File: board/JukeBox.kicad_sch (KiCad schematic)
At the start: 73 parts, among them J1 USB4105-GF-A, J2 Conn_01x03, J3 Conn_01x04, J4 Conn_01x08, J5 Conn_01x01, J6 Conn_01x03, J7 Conn_01x03, J8 Conn_01x01, SW1 SW_SPST, SW10 SW_SPST, SW11 SW_SPST, SW12 SW_SPST, SW2 SW_SPST, SW3 SW_SPST, SW4 SW_SPST, SW5 SW_SPST, SW6 SW_SPST, SW7 SW_SPST, SW8 SW_SPST, SW9 SW_SPST, U1 NCP1117-3.3_SOT223, U2 W25Q128JVS, U3 RP2040, Y1 ABLS-12.000MHZ-B4-T

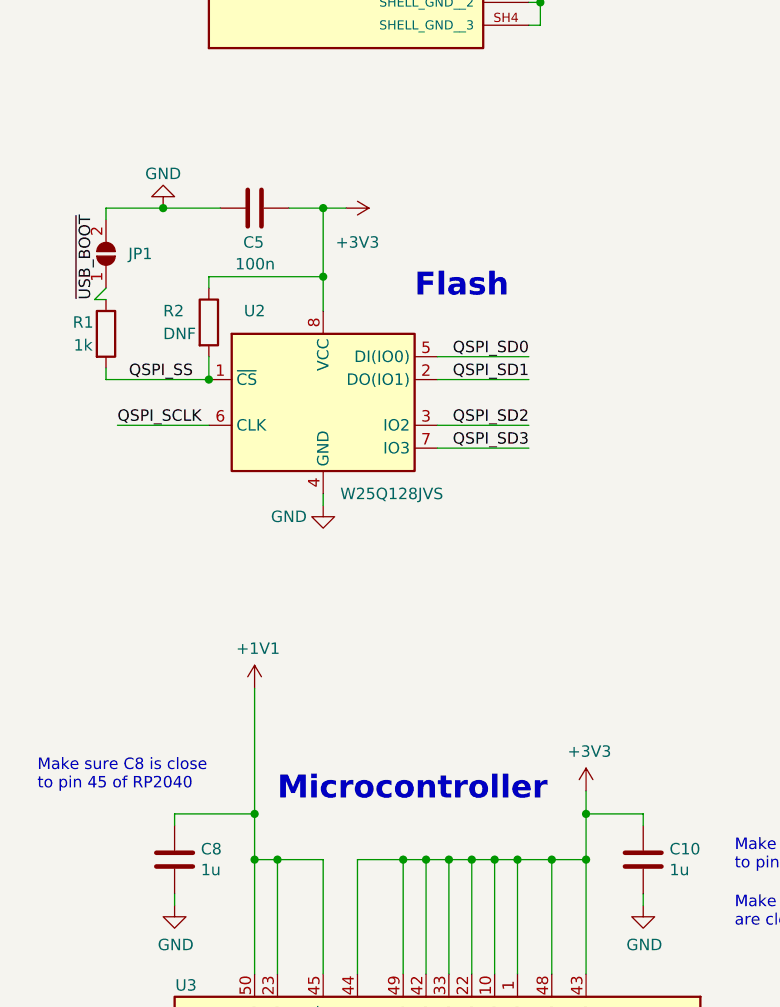
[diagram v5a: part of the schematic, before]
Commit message: change sizes of all the smd's to match parts, remove unnecessary pullup
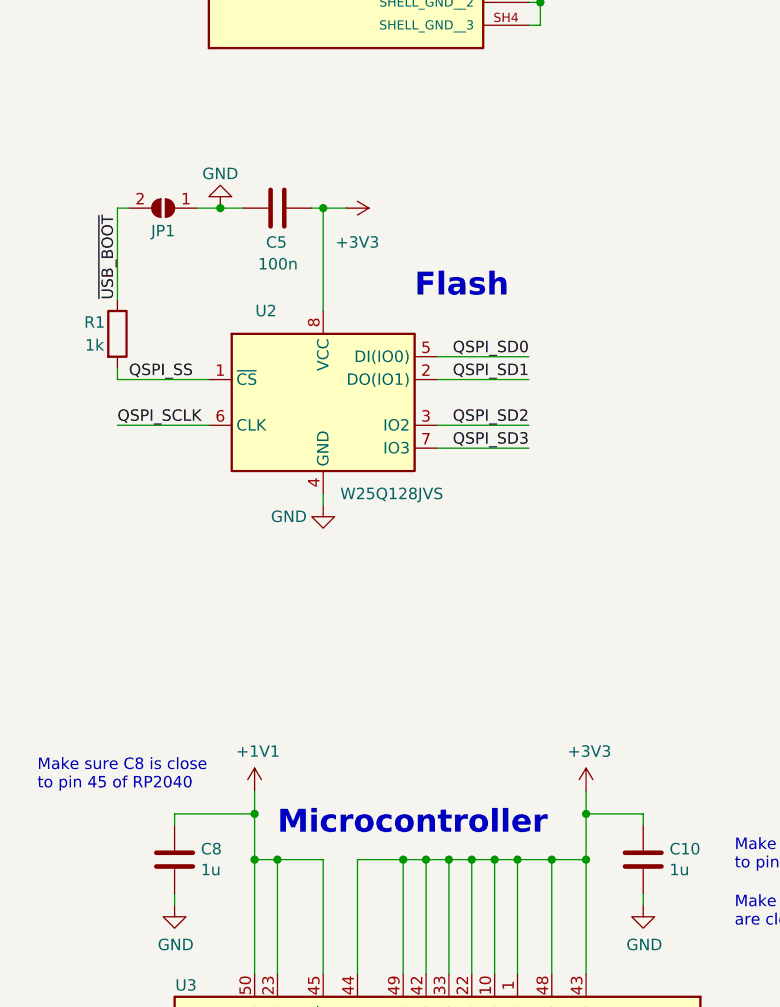
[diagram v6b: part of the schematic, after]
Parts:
- removed R2: DNF, Resistor_SMD:R_1206_3216Metric_Pad1.30x1.75mm_HandSolder, symbol Device:R
- C1, C10, C2, C3, C4, C5, C8: footprint Capacitor_SMD:C_1206_3216Metric_Pad1.33x1.80mm_HandSolder -> Capacitor_SMD:C_0805_2012Metric_Pad1.18x1.45mm_HandSolder
- D1, D10, D11, D12, D2, D3, D4, D5, D6, D7, D8, D9: footprint Diode_SMD:D_1206_3216Metric_Pad1.42x1.75mm_HandSolder -> Diode_SMD:D_SOD-123
- D25: footprint Diode_SMD:D_1206_3216Metric_Pad1.42x1.75mm_HandSolder -> Diode_SMD:D_0805_2012Metric_Pad1.15x1.40mm_HandSolder
- R1, R10, R11, R12, R3, R4, R5, R6, R7, R8, R9: footprint Resistor_SMD:R_1206_3216Metric_Pad1.30x1.75mm_HandSolder -> Resistor_SMD:R_0805_2012Metric_Pad1.20x1.40mm_HandSolder
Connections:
- net GND: now also JP1.1 (A); no longer JP1.2 (B)
- net ~{USB_BOOT}: now also JP1.2 (B); no longer JP1.1 (A)
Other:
- moved on the sheet: C5, JP1, R1

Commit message: fix pcb for new footprints, remove old files, update readme
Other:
- company: Raspberry Pi (Trading) Ltd -> Friend Team Inc.
- title: RP2040 Minimal Design Example -> JukeBoxV5
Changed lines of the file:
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@@
   (paper "A3")
   (title_block
-    (title "RP2040 Minimal Design Example")
-    (date "2020-12-18")
+    (title "JukeBoxV5")
+    (date "2023-12-25")
     (rev "REV1")
-    (company "Raspberry Pi (Trading) Ltd")
+    (company "Friend Team Inc.")
   )
   (junction (at 99.06 31.75) (diameter 0) (color 0 0 0 0)
